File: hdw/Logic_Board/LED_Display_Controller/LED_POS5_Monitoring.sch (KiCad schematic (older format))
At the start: 29 parts, among them J1601 POS5P EXT, J1602 POS5P PGOOD, J1603 POS5P_THWN, J1604 POS5P_RUN, U1601 LM1117-ADJ, U1602 NUP2202, U1603 74LVC1G17, U1604 74LVC1G17, U1605 74LVC1G17, U1606 NUP2202

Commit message: Added some digikey partnumbers to components
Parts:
- C1601: Digi-Key PN (none) -> 478-8236-1-ND
- C1602, C1603, C1605: Digi-Key PN 490-4779-1-ND -> 311-1344-1-ND
- C1604, C1607, C1608, C1609: footprint (none) -> Capacitors_SMD:C_0603; Digi-Key PN PN -> 311-1344-1-ND
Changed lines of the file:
@@
 F 0 "C1604" H 2695 2690 50  0000 L CNN
 F 1 "0.1uF" H 2695 2490 50  0000 L CNN
-F 2 "" H 2708 2440 50  0001 C CNN
+F 2 "Capacitors_SMD:C_0603" H 2708 2440 50  0001 C CNN
 F 3 "" H 2695 2690 50  0001 C CNN
-F 4 "PN" H 3095 3090 60  0001 C CNN "Digi-Key PN"
+F 4 "311-1344-1-ND" H 3095 3090 60  0001 C CNN "Digi-Key PN"
 F 5 "0603" H 2520 2690 50  0000 R CNN "display_footprint"
 F 6 "50V" H 2520 2590 50  0000 R CNN "Voltage"
@@
 F 0 "C1608" H 8225 2800 50  0000 L CNN
 F 1 "0.1uF" H 8225 2600 50  0000 L CNN
-F 2 "" H 8238 2550 50  0001 C CNN
+F 2 "Capacitors_SMD:C_0603" H 8238 2550 50  0001 C CNN
 F 3 "" H 8225 2800 50  0001 C CNN
-F 4 "PN" H 8625 3200 60  0001 C CNN "Digi-Key PN"
+F 4 "311-1344-1-ND" H 8625 3200 60  0001 C CNN "Digi-Key PN"
 F 5 "0603" H 8050 2800 50  0000 R CNN "display_footprint"
 F 6 "50V" H 8050 2700 50  0000 R CNN "Voltage"
@@
 F 0 "C1609" H 8225 4430 50  0000 L CNN
 F 1 "0.1uF" H 8225 4230 50  0000 L CNN
-F 2 "" H 8238 4180 50  0001 C CNN
+F 2 "Capacitors_SMD:C_0603" H 8238 4180 50  0001 C CNN
 F 3 "" H 8225 4430 50  0001 C CNN
-F 4 "PN" H 8625 4830 60  0001 C CNN "Digi-Key PN"
+F 4 "311-1344-1-ND" H 8625 4830 60  0001 C CNN "Digi-Key PN"
 F 5 "0603" H 8050 4430 50  0000 R CNN "display_footprint"
 F 6 "50V" H 8050 4330 50  0000 R CNN "Voltage"
@@
 F 0 "C1607" H 7465 5690 50  0000 L CNN
 F 1 "0.1uF" H 7465 5490 50  0000 L CNN
-F 2 "" H 7478 5440 50  0001 C CNN
+F 2 "Capacitors_SMD:C_0603" H 7478 5440 50  0001 C CNN
 F 3 "" H 7465 5690 50  0001 C CNN
-F 4 "PN" H 7865 6090 60  0001 C CNN "Digi-Key PN"
+F 4 "311-1344-1-ND" H 7865 6090 60  0001 C CNN "Digi-Key PN"
 F 5 "0603" H 7290 5690 50  0000 R CNN "display_footprint"
 F 6 "50V" H 7290 5590 50  0000 R CNN "Voltage"
@@
 F 5 "50V" H 2170 5190 50  0000 R CNN "Voltage"
 F 6 "X7R" H 2170 5090 50  0000 R CNN "Dielectric"
-F 7 "490-4779-1-ND" H 2745 5690 60  0001 C CNN "Digi-Key PN"
+F 7 "311-1344-1-ND" H 2745 5690 60  0001 C CNN "Digi-Key PN"
 	1    2320 5190
 	1    0    0    -1
@@
 F 5 "50V" H 3560 4740 50  0000 R CNN "Voltage"
 F 6 "X7R" H 3560 4640 50  0000 R CNN "Dielectric"
-F 7 "490-4779-1-ND" H 4135 5240 60  0001 C CNN "Digi-Key PN"
+F 7 "311-1344-1-ND" H 4135 5240 60  0001 C CNN "Digi-Key PN"
 	1    3710 4740
 	1    0    0    -1
@@
 F 5 "50V" H 1450 4740 50  0000 R CNN "Voltage"
 F 6 "X7R" H 1450 4640 50  0000 R CNN "Dielectric"
-F 7 "490-4779-1-ND" H 2025 5240 60  0001 C CNN "Digi-Key PN"
+F 7 "311-1344-1-ND" H 2025 5240 60  0001 C CNN "Digi-Key PN"
 	1    1600 4740
 	1    0    0    -1
@@
 F 5 "16V" H 820 4740 50  0000 R CNN "Voltage"
 F 6 "10%" H 820 4640 50  0000 R CNN "Tolerance"
+F 7 "478-8236-1-ND" H 0   0   50  0001 C CNN "Digi-Key PN"
 	1    970  4740
 	1    0    0    -1

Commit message: Finished first pass of digikey part numbers
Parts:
- R1601: Digi-Key PN PN -> RMCF0603FT200RCT-ND
- R1602: Digi-Key PN PN -> P680HCT-ND
- R1603, R1604: Digi-Key PN PN -> RMCF0603FT1K00CT-ND
- R1605, R1606, R1607, R1608, R1609, R1610: Digi-Key PN PN -> RMCF0603FT10K0CT-ND
- U1601: Digi-Key PN (none) -> LM1117IMPX-ADJ/NOPBCT-ND
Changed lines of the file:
@@
 F 5 "1%" V 6590 1980 50  0000 C CNN "Tolerance"
 F 6 "1/10W" V 6690 1980 50  0000 C CNN "Wattage"
-F 7 "PN" H 6690 2380 60  0001 C CNN "Digi-Key PN"
+F 7 "RMCF0603FT1K00CT-ND" H 6690 2380 60  0001 C CNN "Digi-Key PN"
 	1    6390 1980
 	0    1    1    0
@@
 F 5 "1%" V 6590 3610 50  0000 C CNN "Tolerance"
 F 6 "1/10W" V 6690 3610 50  0000 C CNN "Wattage"
-F 7 "PN" H 6690 4010 60  0001 C CNN "Digi-Key PN"
+F 7 "RMCF0603FT1K00CT-ND" H 6690 4010 60  0001 C CNN "Digi-Key PN"
 	1    6390 3610
 	0    1    1    0
@@
 F 5 "1%" H 9310 2180 50  0000 L CNN "Tolerance"
 F 6 "1/10W" H 9310 2110 50  0000 L CNN "Wattage"
-F 7 "PN" H 9510 2580 60  0001 C CNN "Digi-Key PN"
+F 7 "RMCF0603FT10K0CT-ND" H 9510 2580 60  0001 C CNN "Digi-Key PN"
 	1    9210 2180
 	1    0    0    -1
@@
 F 5 "1%" H 9310 3810 50  0000 L CNN "Tolerance"
 F 6 "1/10W" H 9310 3740 50  0000 L CNN "Wattage"
-F 7 "PN" H 9510 4210 60  0001 C CNN "Digi-Key PN"
+F 7 "RMCF0603FT10K0CT-ND" H 9510 4210 60  0001 C CNN "Digi-Key PN"
 	1    9210 3810
 	1    0    0    -1
@@
 F 5 "1%" H 6990 5170 50  0000 L CNN "Tolerance"
 F 6 "1/10W" H 6990 5100 50  0000 L CNN "Wattage"
-F 7 "PN" H 7190 5570 60  0001 C CNN "Digi-Key PN"
+F 7 "RMCF0603FT10K0CT-ND" H 7190 5570 60  0001 C CNN "Digi-Key PN"
 	1    6890 5170
 	1    0    0    -1
@@
 F 2 "" H 2320 4520 50  0001 C CNN
 F 3 "http://www.ti.com/lit/ds/symlink/lm1117.pdf" H 2320 4520 50  0001 C CNN
+F 4 "LM1117IMPX-ADJ/NOPBCT-ND" H 0   0   50  0001 C CNN "Digi-Key PN"
 	1    2320 4520
 	1    0    0    -1
@@
 F 5 "1%" H 3110 4740 50  0000 L CNN "Tolerance"
 F 6 "1/10W" H 3110 4670 50  0000 L CNN "Wattage"
-F 7 "PN" H 3310 5140 60  0001 C CNN "Digi-Key PN"
+F 7 "RMCF0603FT200RCT-ND" H 3310 5140 60  0001 C CNN "Digi-Key PN"
 	1    3010 4740
 	-1   0    0    -1
@@
 F 5 "1%" H 3110 5190 50  0000 L CNN "Tolerance"
 F 6 "1/10W" H 3110 5120 50  0000 L CNN "Wattage"
-F 7 "PN" H 3310 5590 60  0001 C CNN "Digi-Key PN"
+F 7 "P680HCT-ND" H 3310 5590 60  0001 C CNN "Digi-Key PN"
 	1    3010 5190
 	-1   0    0    -1
@@
 F 5 "1%" H 7800 3830 50  0000 L CNN "Tolerance"
 F 6 "1/10W" H 7800 3760 50  0000 L CNN "Wattage"
-F 7 "PN" H 8000 4230 60  0001 C CNN "Digi-Key PN"
+F 7 "RMCF0603FT10K0CT-ND" H 8000 4230 60  0001 C CNN "Digi-Key PN"
 	1    7700 3830
 	1    0    0    -1
@@
 F 5 "1%" H 7800 2200 50  0000 L CNN "Tolerance"
 F 6 "1/10W" H 7800 2130 50  0000 L CNN "Wattage"
-F 7 "PN" H 8000 2600 60  0001 C CNN "Digi-Key PN"
+F 7 "RMCF0603FT10K0CT-ND" H 8000 2600 60  0001 C CNN "Digi-Key PN"
 	1    7700 2200
 	1    0    0    -1
@@
 F 5 "1%" H 8580 5090 50  0000 L CNN "Tolerance"
 F 6 "1/10W" H 8580 5020 50  0000 L CNN "Wattage"
-F 7 "PN" H 8780 5490 60  0001 C CNN "Digi-Key PN"
+F 7 "RMCF0603FT10K0CT-ND" H 8780 5490 60  0001 C CNN "Digi-Key PN"
 	1    8480 5090
 	1    0    0    -1

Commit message: First pass assignment of footprints to all components
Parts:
- C1601, C1606: footprint (none) -> Capacitors_Tantalum_SMD:CP_Tantalum_Case-B_EIA-3528-21_Reflow
- J1601, J1602, J1603, J1604: footprint (none) -> Pin_Headers:Pin_Header_Straight_1x02_Pitch2.54mm
- R1601, R1602, R1603, R1604, R1605, R1606, R1607, R1608, R1609, R1610: footprint (none) -> Resistors_SMD:R_0603
- U1601: footprint (none) -> TO_SOT_Packages_SMD:SOT-223-3_TabPin2
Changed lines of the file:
@@
 F 0 "J1601" H 1840 2532 50  0000 L CNN
 F 1 "POS5P EXT" H 1840 2441 50  0000 L CNN
-F 2 "" H 1760 2540 50  0001 C CNN
+F 2 "Pin_Headers:Pin_Header_Straight_1x02_Pitch2.54mm" H 1760 2540 50  0001 C CNN
 F 3 "~" H 1760 2540 50  0001 C CNN
 	1    1760 2540
@@
 F 0 "J1602" H 5880 1970 50  0000 L CNN
 F 1 "POS5P PGOOD" H 5880 1890 50  0000 L CNN
-F 2 "" H 5780 1980 50  0001 C CNN
+F 2 "Pin_Headers:Pin_Header_Straight_1x02_Pitch2.54mm" H 5780 1980 50  0001 C CNN
 F 3 "~" H 5780 1980 50  0001 C CNN
 	1    5780 1980
@@
 F 0 "R1603" V 6290 1980 50  0000 C CNN
 F 1 "1k" V 6390 1980 50  0000 C CNN
-F 2 "" H 6390 1980 50  0001 C CNN
+F 2 "Resistors_SMD:R_0603" H 6390 1980 50  0001 C CNN
 F 3 "" H 6390 1980 50  0001 C CNN
 F 4 "0603" V 6490 1980 50  0000 C CNN "display_footprint"
@@
 F 0 "J1603" H 5880 3600 50  0000 L CNN
 F 1 "POS5P_THWN" H 5880 3520 50  0000 L CNN
-F 2 "" H 5780 3610 50  0001 C CNN
+F 2 "Pin_Headers:Pin_Header_Straight_1x02_Pitch2.54mm" H 5780 3610 50  0001 C CNN
 F 3 "~" H 5780 3610 50  0001 C CNN
 	1    5780 3610
@@
 F 0 "R1604" V 6290 3610 50  0000 C CNN
 F 1 "1k" V 6390 3610 50  0000 C CNN
-F 2 "" H 6390 3610 50  0001 C CNN
+F 2 "Resistors_SMD:R_0603" H 6390 3610 50  0001 C CNN
 F 3 "" H 6390 3610 50  0001 C CNN
 F 4 "0603" V 6490 3610 50  0000 C CNN "display_footprint"
@@
 F 0 "R1609" H 9150 2180 50  0000 R CNN
 F 1 "10k" V 9210 2180 50  0000 C CNN
-F 2 "" H 9210 2180 50  0001 C CNN
+F 2 "Resistors_SMD:R_0603" H 9210 2180 50  0001 C CNN
 F 3 "" H 9210 2180 50  0001 C CNN
 F 4 "0603" H 9300 2260 50  0000 L CNN "display_footprint"
@@
 F 0 "R1610" H 9150 3810 50  0000 R CNN
 F 1 "10k" V 9210 3810 50  0000 C CNN
-F 2 "" H 9210 3810 50  0001 C CNN
+F 2 "Resistors_SMD:R_0603" H 9210 3810 50  0001 C CNN
 F 3 "" H 9210 3810 50  0001 C CNN
 F 4 "0603" H 9300 3890 50  0000 L CNN "display_footprint"
@@
 F 0 "J1604" H 9889 4862 50  0000 L CNN
 F 1 "POS5P_RUN" H 9889 4771 50  0000 L CNN
-F 2 "" H 9810 4870 50  0001 C CNN
+F 2 "Pin_Headers:Pin_Header_Straight_1x02_Pitch2.54mm" H 9810 4870 50  0001 C CNN
 F 3 "~" H 9810 4870 50  0001 C CNN
 	1    9810 4870
@@
 F 0 "R1605" H 6830 5170 50  0000 R CNN
 F 1 "10k" V 6890 5170 50  0000 C CNN
-F 2 "" H 6890 5170 50  0001 C CNN
+F 2 "Resistors_SMD:R_0603" H 6890 5170 50  0001 C CNN
 F 3 "" H 6890 5170 50  0001 C CNN
 F 4 "0603" H 6980 5250 50  0000 L CNN "display_footprint"
@@
 F 0 "U1601" H 2170 4645 50  0000 C CNN
 F 1 "LM1117-ADJ" H 2320 4645 50  0000 L CNN
-F 2 "" H 2320 4520 50  0001 C CNN
+F 2 "TO_SOT_Packages_SMD:SOT-223-3_TabPin2" H 2320 4520 50  0001 C CNN
 F 3 "http://www.ti.com/lit/ds/symlink/lm1117.pdf" H 2320 4520 50  0001 C CNN
 F 4 "LM1117IMPX-ADJ/NOPBCT-ND" H 0   0   50  0001 C CNN "Digi-Key PN"
@@
 F 0 "R1601" H 2950 4740 50  0000 R CNN
 F 1 "200" V 3010 4740 50  0000 C CNN
-F 2 "" H 3010 4740 50  0001 C CNN
+F 2 "Resistors_SMD:R_0603" H 3010 4740 50  0001 C CNN
 F 3 "" H 3010 4740 50  0001 C CNN
 F 4 "0603" H 3100 4820 50  0000 L CNN "display_footprint"
@@
 F 0 "R1602" H 2950 5190 50  0000 R CNN
 F 1 "680" V 3010 5190 50  0000 C CNN
-F 2 "" H 3010 5190 50  0001 C CNN
+F 2 "Resistors_SMD:R_0603" H 3010 5190 50  0001 C CNN
 F 3 "" H 3010 5190 50  0001 C CNN
 F 4 "0603" H 3100 5270 50  0000 L CNN "display_footprint"
@@
 F 0 "C1601" H 995 4840 50  0000 L CNN
 F 1 "10uF" H 995 4640 50  0000 L CNN
-F 2 "" H 1008 4590 50  0001 C CNN
+F 2 "Capacitors_Tantalum_SMD:CP_Tantalum_Case-B_EIA-3528-21_Reflow" H 1008 4590 50  0001 C CNN
 F 3 "" H 995 4840 50  0001 C CNN
 F 4 "3528" H 820 4840 50  0000 R CNN "display_footprint"
@@
 F 0 "C1606" H 4535 4840 50  0000 L CNN
 F 1 "100uF" H 4535 4640 50  0000 L CNN
-F 2 "" H 4548 4590 50  0001 C CNN
+F 2 "Capacitors_Tantalum_SMD:CP_Tantalum_Case-B_EIA-3528-21_Reflow" H 4548 4590 50  0001 C CNN
 F 3 "" H 4535 4840 50  0001 C CNN
 F 4 "399-5306-1-ND" H 4510 4740 50  0001 C CNN "Digi-Key PN"
@@
 F 0 "R1607" H 7640 3830 50  0000 R CNN
 F 1 "10k" V 7700 3830 50  0000 C CNN
-F 2 "" H 7700 3830 50  0001 C CNN
+F 2 "Resistors_SMD:R_0603" H 7700 3830 50  0001 C CNN
 F 3 "" H 7700 3830 50  0001 C CNN
 F 4 "0603" H 7790 3910 50  0000 L CNN "display_footprint"
@@
 F 0 "R1606" H 7640 2200 50  0000 R CNN
 F 1 "10k" V 7700 2200 50  0000 C CNN
-F 2 "" H 7700 2200 50  0001 C CNN
+F 2 "Resistors_SMD:R_0603" H 7700 2200 50  0001 C CNN
 F 3 "" H 7700 2200 50  0001 C CNN
 F 4 "0603" H 7790 2280 50  0000 L CNN "display_footprint"
@@
 F 0 "R1608" H 8420 5090 50  0000 R CNN
 F 1 "10k" V 8480 5090 50  0000 C CNN
-F 2 "" H 8480 5090 50  0001 C CNN
+F 2 "Resistors_SMD:R_0603" H 8480 5090 50  0001 C CNN
 F 3 "" H 8480 5090 50  0001 C CNN
 F 4 "0603" H 8570 5170 50  0000 L CNN "display_footprint"

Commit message: Resolved a few library dependencies
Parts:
- R1603, R1604: symbol Custom_Library:R_Custom -> LED_Display_Local_Library:R_Custom
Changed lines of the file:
@@
 $EndComp
 $Comp
-L Custom_Library:+5.5V #PWR01629
+L LED_Display_Local_Library:+5.5V #PWR01629
 U 1 1 5BEA3712
 P 8350 1880
@@
 $EndComp
 $Comp
-L Custom_Library:R_Custom R1603
+L LED_Display_Local_Library:R_Custom R1603
 U 1 1 5BEAE5DF
 P 6390 1980
@@
 $EndComp
 $Comp
-L Custom_Library:+5.5V #PWR01631
+L LED_Display_Local_Library:+5.5V #PWR01631
 U 1 1 5BEB81A9
 P 8350 3510
@@
 $EndComp
 $Comp
-L Custom_Library:R_Custom R1604
+L LED_Display_Local_Library:R_Custom R1604
 U 1 1 5BEB81DD
 P 6390 3610
@@
 $EndComp
 $Comp
-L Custom_Library:+5.5V #PWR01621
+L LED_Display_Local_Library:+5.5V #PWR01621
 U 1 1 5BF0EF00
 P 7590 4770

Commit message: Modified BOM
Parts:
- C1606: Digi-Key PN 399-5306-1-ND -> 478-3130-1-ND
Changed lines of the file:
@@
 F 2 "Capacitors_Tantalum_SMD:CP_Tantalum_Case-B_EIA-3528-21_Reflow" H 4548 4590 50  0001 C CNN
 F 3 "" H 4535 4840 50  0001 C CNN
-F 4 "399-5306-1-ND" H 4510 4740 50  0001 C CNN "Digi-Key PN"
+F 4 "478-3130-1-ND" H 4510 4740 50  0001 C CNN "Digi-Key PN"
 F 5 "3528" H 4360 4840 50  0000 R CNN "display_footprint"
 F 6 "6.3V" H 4360 4740 50  0000 R CNN "Voltage"

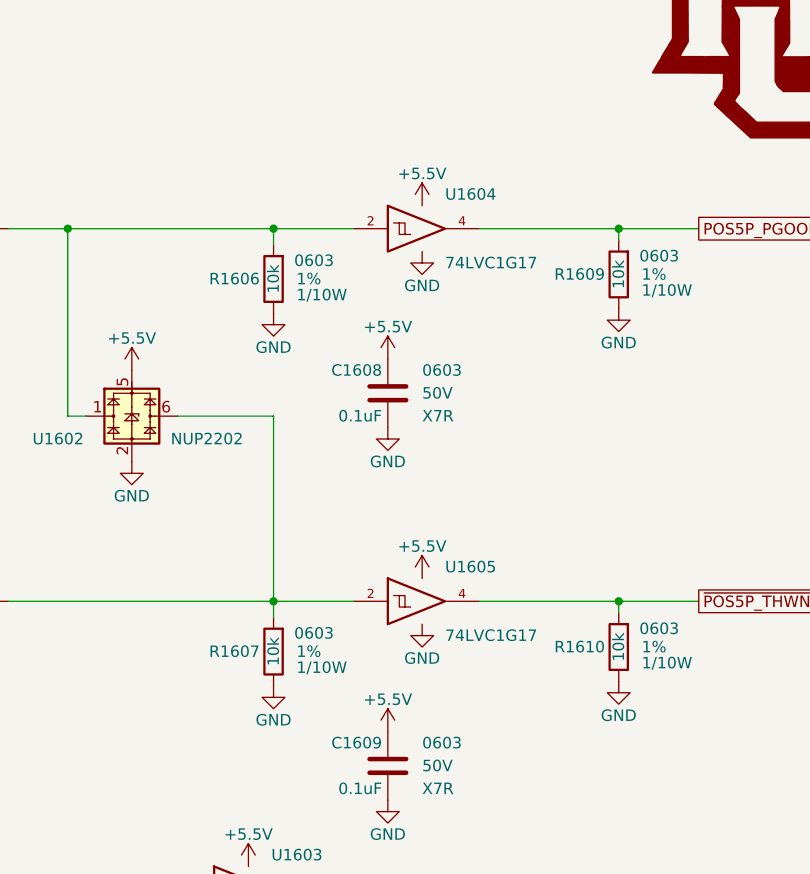
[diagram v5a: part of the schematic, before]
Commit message: arranged rotary encoder parts
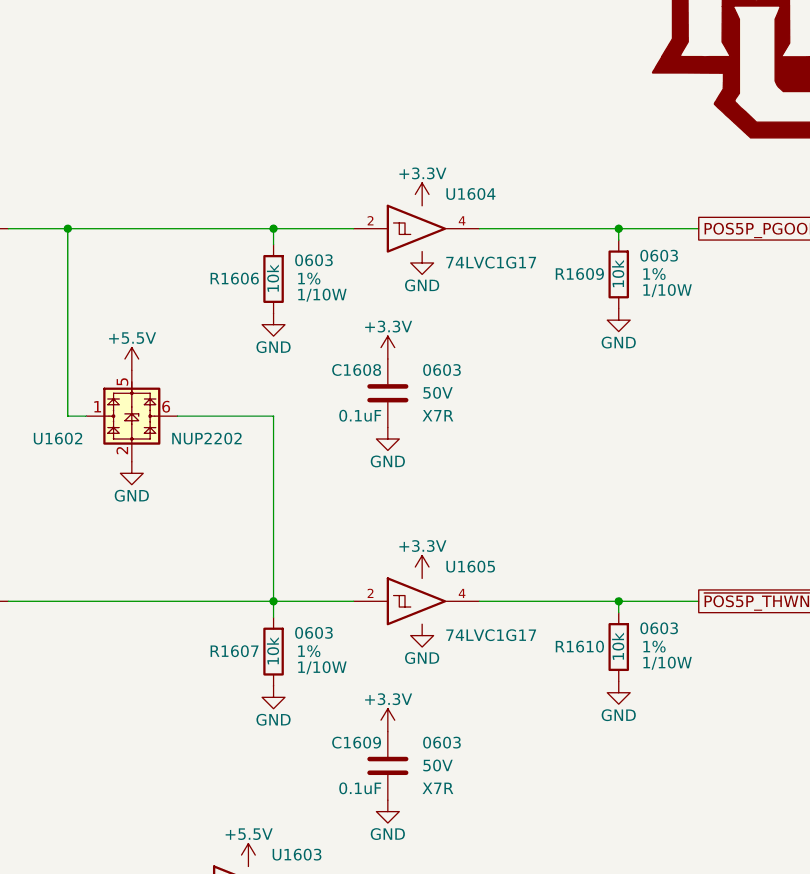
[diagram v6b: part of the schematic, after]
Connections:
- net +5.5V: no longer C1608.1, C1609.1, U1604.5 (VCC), U1605.5 (VCC)
- new net +3V3: C1608.1, C1609.1, U1604.5 (VCC), U1605.5 (VCC)
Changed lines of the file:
@@
-$EndComp
-$Comp
-L LED_Display_Local_Library:+5.5V #PWR01629
-U 1 1 5BEA3712
-P 8350 1880
-F 0 "#PWR01629" H 8350 1730 50  0001 C CNN
-F 1 "+5.5V" H 8350 2020 50  0000 C CNN
-F 2 "" H 8350 1880 50  0001 C CNN
-F 3 "" H 8350 1880 50  0001 C CNN
-	1    8350 1880
-	1    0    0    -1
 $EndComp
 $Comp
@@
 $EndComp
 $Comp
-L LED_Display_Local_Library:+5.5V #PWR01625
-U 1 1 5BEA37E6
-P 8200 2550
-F 0 "#PWR01625" H 8200 2400 50  0001 C CNN
-F 1 "+5.5V" H 8200 2690 50  0000 C CNN
-F 2 "" H 8200 2550 50  0001 C CNN
-F 3 "" H 8200 2550 50  0001 C CNN
-	1    8200 2550
-	1    0    0    -1
-$EndComp
-$Comp
 L power:GND #PWR01618
 U 1 1 5BEA85AB
@@
 F 3 "" H 8350 3710 50  0001 C CNN
 	1    8350 3710
-	1    0    0    -1
-$EndComp
-$Comp
-L LED_Display_Local_Library:+5.5V #PWR01631
-U 1 1 5BEB81A9
-P 8350 3510
-F 0 "#PWR01631" H 8350 3360 50  0001 C CNN
-F 1 "+5.5V" H 8350 3650 50  0000 C CNN
-F 2 "" H 8350 3510 50  0001 C CNN
-F 3 "" H 8350 3510 50  0001 C CNN
-	1    8350 3510
 	1    0    0    -1
 $EndComp
@@
 F 3 "" H 8200 4480 50  0001 C CNN
 	1    8200 4480
-	1    0    0    -1
-$EndComp
-$Comp
-L LED_Display_Local_Library:+5.5V #PWR01627
-U 1 1 5BEB81C0
-P 8200 4180
-F 0 "#PWR01627" H 8200 4030 50  0001 C CNN
-F 1 "+5.5V" H 8200 4320 50  0000 C CNN
-F 2 "" H 8200 4180 50  0001 C CNN
-F 3 "" H 8200 4180 50  0001 C CNN
-	1    8200 4180
 	1    0    0    -1
 $EndComp
@@
 Wire Wire Line
 	8600 3610 9210 3610
+$Comp
+L power:+3.3V #PWR?
+U 1 1 5C0DE1C0
+P 8350 1880
+F 0 "#PWR?" H 8350 1730 50  0001 C CNN
+F 1 "+3.3V" H 8350 2020 50  0000 C CNN
+F 2 "" H 8350 1880 50  0001 C CNN
+F 3 "" H 8350 1880 50  0001 C CNN
+	1    8350 1880
+	1    0    0    -1
+$EndComp
+$Comp
+L power:+3.3V #PWR?
+U 1 1 5C0DE394
+P 8200 2550
+F 0 "#PWR?" H 8200 2400 50  0001 C CNN
+F 1 "+3.3V" H 8200 2690 50  0000 C CNN
+F 2 "" H 8200 2550 50  0001 C CNN
+F 3 "" H 8200 2550 50  0001 C CNN
+	1    8200 2550
+	1    0    0    -1
+$EndComp
+$Comp
+L power:+3.3V #PWR?
+U 1 1 5C0DE44D
+P 8350 3510
+F 0 "#PWR?" H 8350 3360 50  0001 C CNN
+F 1 "+3.3V" H 8350 3650 50  0000 C CNN
+F 2 "" H 8350 3510 50  0001 C CNN
+F 3 "" H 8350 3510 50  0001 C CNN
+	1    8350 3510
+	1    0    0    -1
+$EndComp
+$Comp
+L power:+3.3V #PWR?
+U 1 1 5C0DE57A
+P 8200 4180
+F 0 "#PWR?" H 8200 4030 50  0001 C CNN
+F 1 "+3.3V" H 8200 4320 50  0000 C CNN
+F 2 "" H 8200 4180 50  0001 C CNN
+F 3 "" H 8200 4180 50  0001 C CNN
+	1    8200 4180
+	1    0    0    -1
+$EndComp
 $EndSCHEMATC

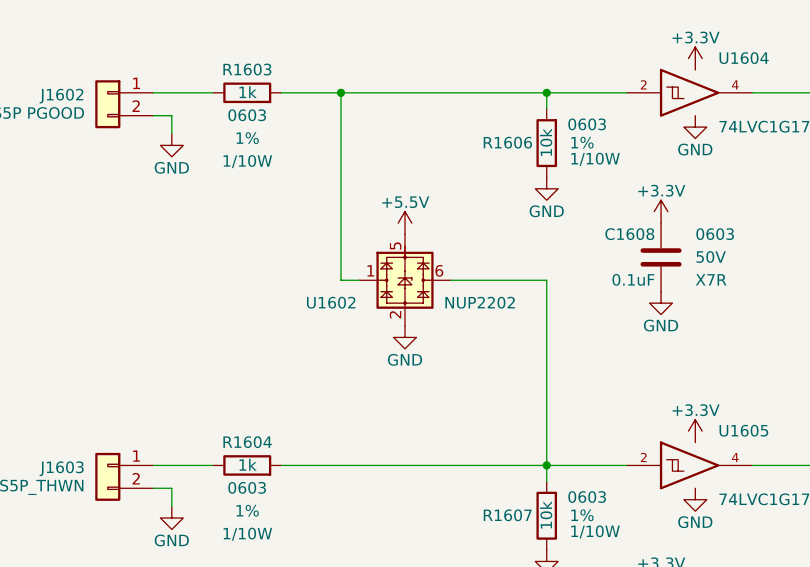
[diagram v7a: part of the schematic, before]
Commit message: Fixed net placement on level shifters, lots of part placements on PCB
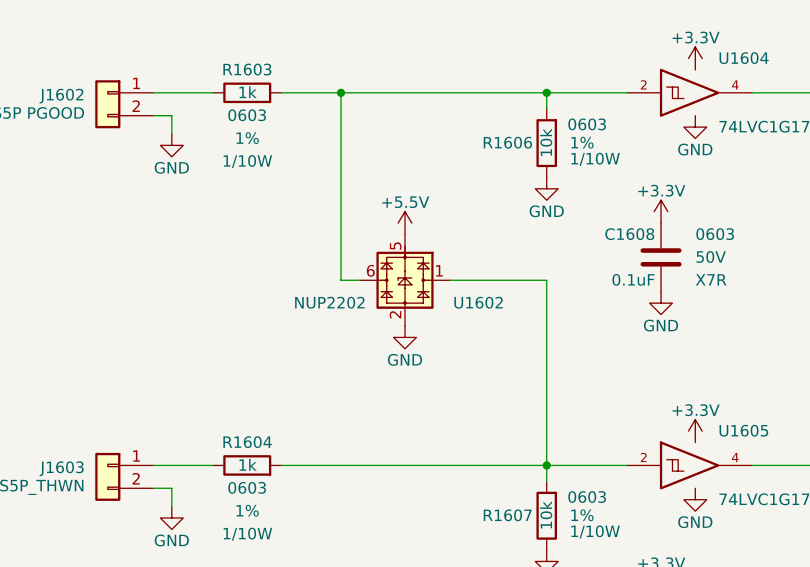
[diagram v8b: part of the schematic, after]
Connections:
- net at R1603.1, R1606.1, U1604.2: now also U1602.6; no longer U1602.1
- net at R1604.1, R1607.1, U1605.2: now also U1602.1; no longer U1602.6
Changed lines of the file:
@@
 F 4 "NUP2202W1T2GOSCT-ND" H 7080 2800 50  0001 C CNN "Digi-Key PN"
 	1    7080 2800
-	1    0    0    -1
+	-1   0    0    -1
 $EndComp
 Wire Wire Line
